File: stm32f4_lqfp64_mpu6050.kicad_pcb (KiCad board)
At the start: 4 copper layers, 130 x 100 mm, 170 parts, among them M5 ALIS-CUSTOM-PARTS_POWERPADS, P1 CONN_01X08, P2 CONN_02X08, Q5 BSS138, Q6 CRYSTAL_50X32, U1 STM32F405R, U2 MPU6050, U3 LP2985LV, U4 LP2985LV, U5 W25Q80BV, U6 LM1881, U7 TS5A3160, U8 TS5A3160, X1 CON-JST_SM04B-SRSS-TB, X2 CON-JST_SM04B-SRSS-TB, X4 CON-JST_SM04B-SRSS-TB

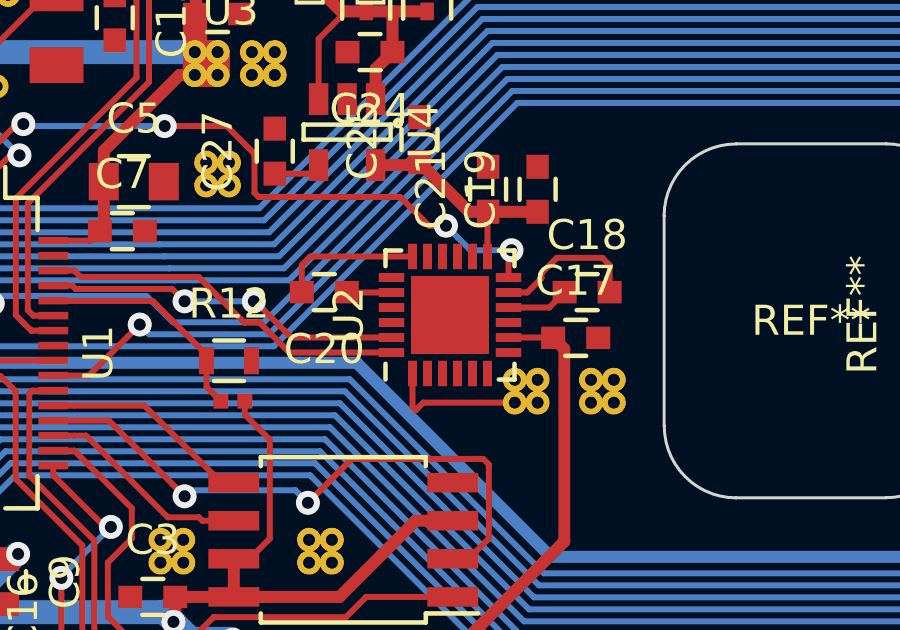
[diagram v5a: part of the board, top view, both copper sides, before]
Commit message: deleted the ground pad under the mpu6050
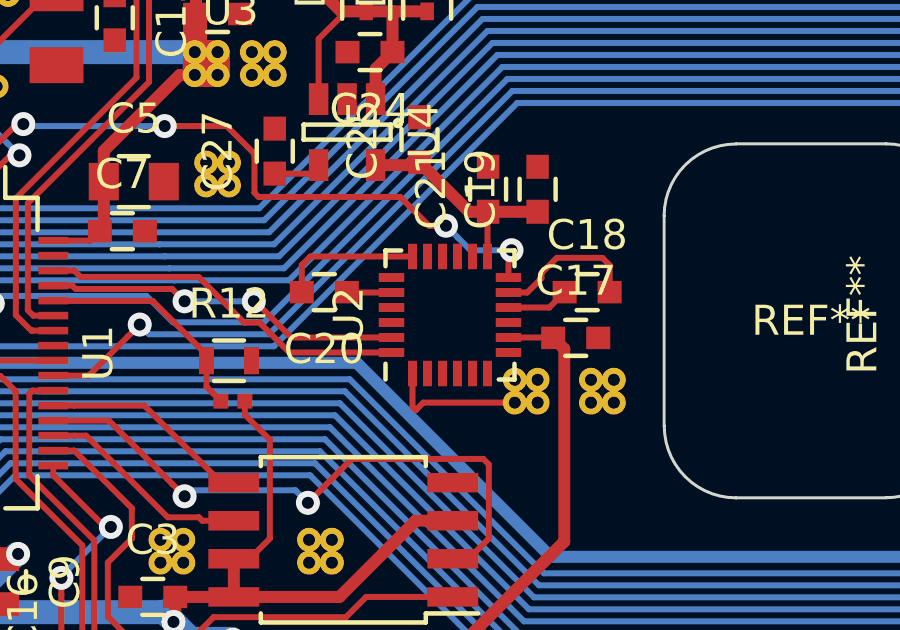
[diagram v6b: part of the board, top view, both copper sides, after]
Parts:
- U2: footprint Housings_DFN_QFN:QFN-24-1EP_4x4mm_Pitch0.5mm -> QFN-24_4x4mm_Pitch0.5mm
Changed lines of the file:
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@@
     (add_net VBAT)
+  )
+  (module QFN-24_4x4mm_Pitch0.5mm (layer Top)
+    (at 132.08 104.775 90)
+    (descr "24-Lead Plastic Quad Flat, No Lead Package (MJ) - 4x4x0.9 mm Body [QFN]; (see Microchip Packaging Specification 00000049BS.pdf)")
+    (tags "QFN 0.5")
+    (attr smd)
+    (fp_text reference U2 (at 0 -3.375 90) (layer F.SilkS)
+      (effects (font (size 1 1) (thickness 0.15)))
+    )
+    (fp_text value MPU6050 (at 0 3.375 90) (layer F.Fab)
+      (effects (font (size 1 1) (thickness 0.15)))
+    )
+    (fp_line (start -2.65 -2.65) (end -2.65 2.65) (layer F.CrtYd) (width 0.05))
+    (fp_line (start 2.65 -2.65) (end 2.65 2.65) (layer F.CrtYd) (width 0.05))
+    (fp_line (start -2.65 -2.65) (end 2.65 -2.65) (layer F.CrtYd) (width 0.05))
+    (fp_line (start -2.65 2.65) (end 2.65 2.65) (layer F.CrtYd) (width 0.05))
+    (fp_line (start 2.15 -2.15) (end 2.15 -1.625) (layer F.SilkS) (width 0.15))
+    (fp_line (start -2.15 2.15) (end -2.15 1.625) (layer F.SilkS) (width 0.15))
+    (fp_line (start 2.15 2.15) (end 2.15 1.625) (layer F.SilkS) (width 0.15))
+    (fp_line (start -2.15 -2.15) (end -1.625 -2.15) (layer F.SilkS) (width 0.15))
+    (fp_line (start -2.15 2.15) (end -1.625 2.15) (layer F.SilkS) (width 0.15))
+    (fp_line (start 2.15 2.15) (end 1.625 2.15) (layer F.SilkS) (width 0.15))
+    (fp_line (start 2.15 -2.15) (end 1.625 -2.15) (layer F.SilkS) (width 0.15))
+    (pad 1 smd rect (at -1.95 -1.25 90) (size 0.85 0.3) (layers Top F.Paste F.Mask)
+      (net 1 GND))
+    (pad 2 smd rect (at -1.95 -0.75 90) (size 0.85 0.3) (layers Top F.Paste F.Mask)
+      (net 68 "Net-(U2-Pad2)"))
+    (pad 3 smd rect (at -1.95 -0.25 90) (size 0.85 0.3) (layers Top F.Paste F.Mask)
+      (net 69 "Net-(U2-Pad3)"))
+    (pad 4 smd rect (at -1.95 0.25 90) (size 0.85 0.3) (layers Top F.Paste F.Mask)
+      (net 70 "Net-(U2-Pad4)"))
+    (pad 5 smd rect (at -1.95 0.75 90) (size 0.85 0.3) (layers Top F.Paste F.Mask)
+      (net 71 "Net-(U2-Pad5)"))
+    (pad 6 smd rect (at -1.95 1.25 90) (size 0.85 0.3) (layers Top F.Paste F.Mask)
+      (net 72 "Net-(U2-Pad6)"))
+    (pad 7 smd rect (at -1.25 1.95 180) (size 0.85 0.3) (layers Top F.Paste F.Mask)
+      (net 73 "Net-(U2-Pad7)"))
+    (pad 8 smd rect (at -0.75 1.95 180) (size 0.85 0.3) (layers Top F.Paste F.Mask)
+      (net 3 3.3V))
+    (pad 9 smd rect (at -0.25 1.95 180) (size 0.85 0.3) (layers Top F.Paste F.Mask)
+      (net 74 "Net-(U2-Pad9)"))
+    (pad 10 smd rect (at 0.25 1.95 180) (size 0.85 0.3) (layers Top F.Paste F.Mask)
+      (net 9 "Net-(C18-Pad1)"))
+    (pad 11 smd rect (at 0.75 1.95 180) (size 0.85 0.3) (layers Top F.Paste F.Mask)
+      (net 1 GND))
+    (pad 12 smd rect (at 1.25 1.95 180) (size 0.85 0.3) (layers Top F.Paste F.Mask)
+      (net 37 IMU_INT))
+    (pad 13 smd rect (at 1.95 1.25 90) (size 0.85 0.3) (layers Top F.Paste F.Mask)
+      (net 10 3.3V_SEN))
+    (pad 14 smd rect (at 1.95 0.75 90) (size 0.85 0.3) (layers Top F.Paste F.Mask)
+      (net 75 "Net-(U2-Pad14)"))
+    (pad 15 smd rect (at 1.95 0.25 90) (size 0.85 0.3) (layers Top F.Paste F.Mask)
+      (net 76 "Net-(U2-Pad15)"))
+    (pad 16 smd rect (at 1.95 -0.25 90) (size 0.85 0.3) (layers Top F.Paste F.Mask)
+      (net 77 "Net-(U2-Pad16)"))
+    (pad 17 smd rect (at 1.95 -0.75 90) (size 0.85 0.3) (layers Top F.Paste F.Mask)
+      (net 78 "Net-(U2-Pad17)"))
+    (pad 18 smd rect (at 1.95 -1.25 90) (size 0.85 0.3) (layers Top F.Paste F.Mask)
+      (net 1 GND))
+    (pad 19 smd rect (at 1.25 -1.95 180) (size 0.85 0.3) (layers Top F.Paste F.Mask)
+      (net 79 "Net-(U2-Pad19)"))
+    (pad 20 smd rect (at 0.75 -1.95 180) (size 0.85 0.3) (layers Top F.Paste F.Mask)
+      (net 11 "Net-(C20-Pad1)"))
+    (pad 21 smd rect (at 0.25 -1.95 180) (size 0.85 0.3) (layers Top F.Paste F.Mask)
+      (net 80 "Net-(U2-Pad21)"))
+    (pad 22 smd rect (at -0.25 -1.95 180) (size 0.85 0.3) (layers Top F.Paste F.Mask)
+      (net 81 "Net-(U2-Pad22)"))
+    (pad 23 smd rect (at -0.75 -1.95 180) (size 0.85 0.3) (layers Top F.Paste F.Mask)
+      (net 66 SCL))
+    (pad 24 smd rect (at -1.25 -1.95 180) (size 0.85 0.3) (layers Top F.Paste F.Mask)
+      (net 67 SDA))
+    (model Housings_DFN_QFN.3dshapes/QFN-24-1EP_4x4mm_Pitch0.5mm.wrl
+      (at (xyz 0 0 0))
+      (scale (xyz 1 1 1))
+      (rotate (xyz 0 0 0))
+    )
   )
   (module alis_parts:via_04 (layer Top)
@@
       (at (xyz 0 0 0))
       (scale (xyz 1 1 1))
-      (rotate (xyz 0 0 0))
-    )
-  )
-  (module Housings_DFN_QFN:QFN-24-1EP_4x4mm_Pitch0.5mm (layer Top)
-    (at 132.08 104.775 90)
-    (descr "24-Lead Plastic Quad Flat, No Lead Package (MJ) - 4x4x0.9 mm Body [QFN]; (see Microchip Packaging Specification 00000049BS.pdf)")
-    (tags "QFN 0.5")
-    (attr smd)
-    (fp_text reference U2 (at 0 -3.375 90) (layer F.SilkS)
-      (effects (font (size 1 1) (thickness 0.15)))
-    )
-    (fp_text value MPU6050 (at 0 3.375 90) (layer F.Fab)
-      (effects (font (size 1 1) (thickness 0.15)))
-    )
-    (fp_line (start -2.65 -2.65) (end -2.65 2.65) (layer F.CrtYd) (width 0.05))
-    (fp_line (start 2.65 -2.65) (end 2.65 2.65) (layer F.CrtYd) (width 0.05))
-    (fp_line (start -2.65 -2.65) (end 2.65 -2.65) (layer F.CrtYd) (width 0.05))
-    (fp_line (start -2.65 2.65) (end 2.65 2.65) (layer F.CrtYd) (width 0.05))
-    (fp_line (start 2.15 -2.15) (end 2.15 -1.625) (layer F.SilkS) (width 0.15))
-    (fp_line (start -2.15 2.15) (end -2.15 1.625) (layer F.SilkS) (width 0.15))
-    (fp_line (start 2.15 2.15) (end 2.15 1.625) (layer F.SilkS) (width 0.15))
-    (fp_line (start -2.15 -2.15) (end -1.625 -2.15) (layer F.SilkS) (width 0.15))
-    (fp_line (start -2.15 2.15) (end -1.625 2.15) (layer F.SilkS) (width 0.15))
-    (fp_line (start 2.15 2.15) (end 1.625 2.15) (layer F.SilkS) (width 0.15))
-    (fp_line (start 2.15 -2.15) (end 1.625 -2.15) (layer F.SilkS) (width 0.15))
-    (pad 1 smd rect (at -1.95 -1.25 90) (size 0.85 0.3) (layers Top F.Paste F.Mask)
-      (net 1 GND))
-    (pad 2 smd rect (at -1.95 -0.75 90) (size 0.85 0.3) (layers Top F.Paste F.Mask)
-      (net 68 "Net-(U2-Pad2)"))
-    (pad 3 smd rect (at -1.95 -0.25 90) (size 0.85 0.3) (layers Top F.Paste F.Mask)
-      (net 69 "Net-(U2-Pad3)"))
-    (pad 4 smd rect (at -1.95 0.25 90) (size 0.85 0.3) (layers Top F.Paste F.Mask)
-      (net 70 "Net-(U2-Pad4)"))
-    (pad 5 smd rect (at -1.95 0.75 90) (size 0.85 0.3) (layers Top F.Paste F.Mask)
-      (net 71 "Net-(U2-Pad5)"))
-    (pad 6 smd rect (at -1.95 1.25 90) (size 0.85 0.3) (layers Top F.Paste F.Mask)
-      (net 72 "Net-(U2-Pad6)"))
-    (pad 7 smd rect (at -1.25 1.95 180) (size 0.85 0.3) (layers Top F.Paste F.Mask)
-      (net 73 "Net-(U2-Pad7)"))
-    (pad 8 smd rect (at -0.75 1.95 180) (size 0.85 0.3) (layers Top F.Paste F.Mask)
-      (net 3 3.3V))
-    (pad 9 smd rect (at -0.25 1.95 180) (size 0.85 0.3) (layers Top F.Paste F.Mask)
-      (net 74 "Net-(U2-Pad9)"))
-    (pad 10 smd rect (at 0.25 1.95 180) (size 0.85 0.3) (layers Top F.Paste F.Mask)
-      (net 9 "Net-(C18-Pad1)"))
-    (pad 11 smd rect (at 0.75 1.95 180) (size 0.85 0.3) (layers Top F.Paste F.Mask)
-      (net 1 GND))
-    (pad 12 smd rect (at 1.25 1.95 180) (size 0.85 0.3) (layers Top F.Paste F.Mask)
-      (net 37 IMU_INT))
-    (pad 13 smd rect (at 1.95 1.25 90) (size 0.85 0.3) (layers Top F.Paste F.Mask)
-      (net 10 3.3V_SEN))
-    (pad 14 smd rect (at 1.95 0.75 90) (size 0.85 0.3) (layers Top F.Paste F.Mask)
-      (net 75 "Net-(U2-Pad14)"))
-    (pad 15 smd rect (at 1.95 0.25 90) (size 0.85 0.3) (layers Top F.Paste F.Mask)
-      (net 76 "Net-(U2-Pad15)"))
-    (pad 16 smd rect (at 1.95 -0.25 90) (size 0.85 0.3) (layers Top F.Paste F.Mask)
-      (net 77 "Net-(U2-Pad16)"))
-    (pad 17 smd rect (at 1.95 -0.75 90) (size 0.85 0.3) (layers Top F.Paste F.Mask)
-      (net 78 "Net-(U2-Pad17)"))
-    (pad 18 smd rect (at 1.95 -1.25 90) (size 0.85 0.3) (layers Top F.Paste F.Mask)
-      (net 1 GND))
-    (pad 19 smd rect (at 1.25 -1.95 180) (size 0.85 0.3) (layers Top F.Paste F.Mask)
-      (net 79 "Net-(U2-Pad19)"))
-    (pad 20 smd rect (at 0.75 -1.95 180) (size 0.85 0.3) (layers Top F.Paste F.Mask)
-      (net 11 "Net-(C20-Pad1)"))
-    (pad 21 smd rect (at 0.25 -1.95 180) (size 0.85 0.3) (layers Top F.Paste F.Mask)
-      (net 80 "Net-(U2-Pad21)"))
-    (pad 22 smd rect (at -0.25 -1.95 180) (size 0.85 0.3) (layers Top F.Paste F.Mask)
-      (net 81 "Net-(U2-Pad22)"))
-    (pad 23 smd rect (at -0.75 -1.95 180) (size 0.85 0.3) (layers Top F.Paste F.Mask)
-      (net 66 SCL))
-    (pad 24 smd rect (at -1.25 -1.95 180) (size 0.85 0.3) (layers Top F.Paste F.Mask)
-      (net 67 SDA))
-    (pad 25 smd rect (at 0.65 0.65 90) (size 1.3 1.3) (layers Top F.Paste F.Mask)
-      (solder_paste_margin_ratio -0.2))
-    (pad 25 smd rect (at 0.65 -0.65 90) (size 1.3 1.3) (layers Top F.Paste F.Mask)
-      (solder_paste_margin_ratio -0.2))
-    (pad 25 smd rect (at -0.65 0.65 90) (size 1.3 1.3) (layers Top F.Paste F.Mask)
-      (solder_paste_margin_ratio -0.2))
-    (pad 25 smd rect (at -0.65 -0.65 90) (size 1.3 1.3) (layers Top F.Paste F.Mask)
-      (solder_paste_margin_ratio -0.2))
-    (model Housings_DFN_QFN.3dshapes/QFN-24-1EP_4x4mm_Pitch0.5mm.wrl
-      (at (xyz 0 0 0))
-      (scale (xyz 1 1 1))

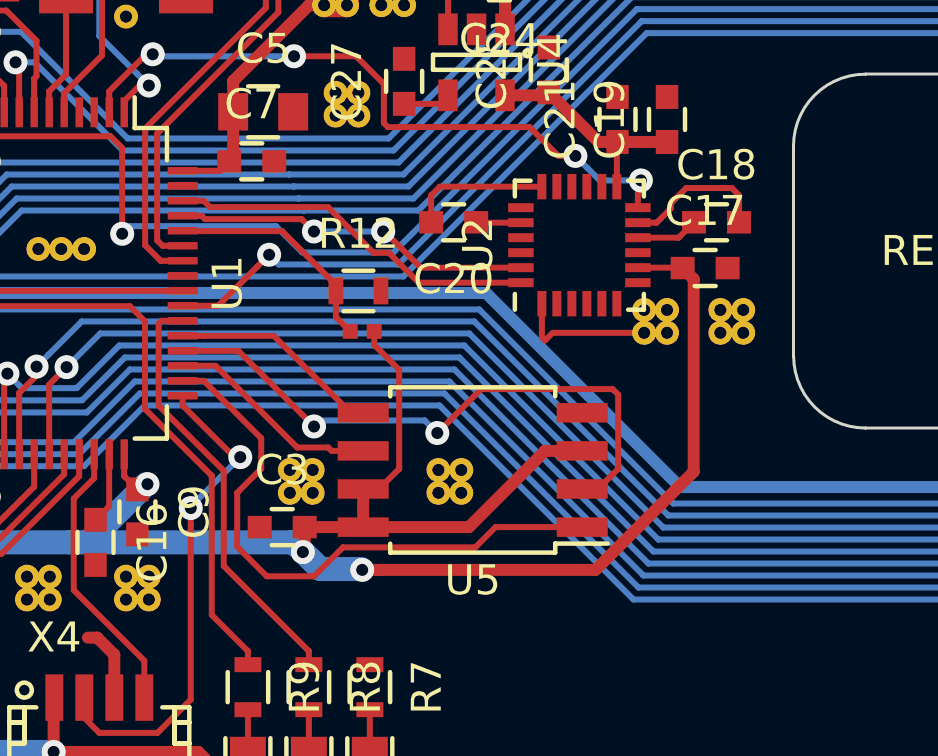
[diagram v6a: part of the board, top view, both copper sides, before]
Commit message: added I2C pullups and pulled MPU6050 AD0 to GND (DOH)
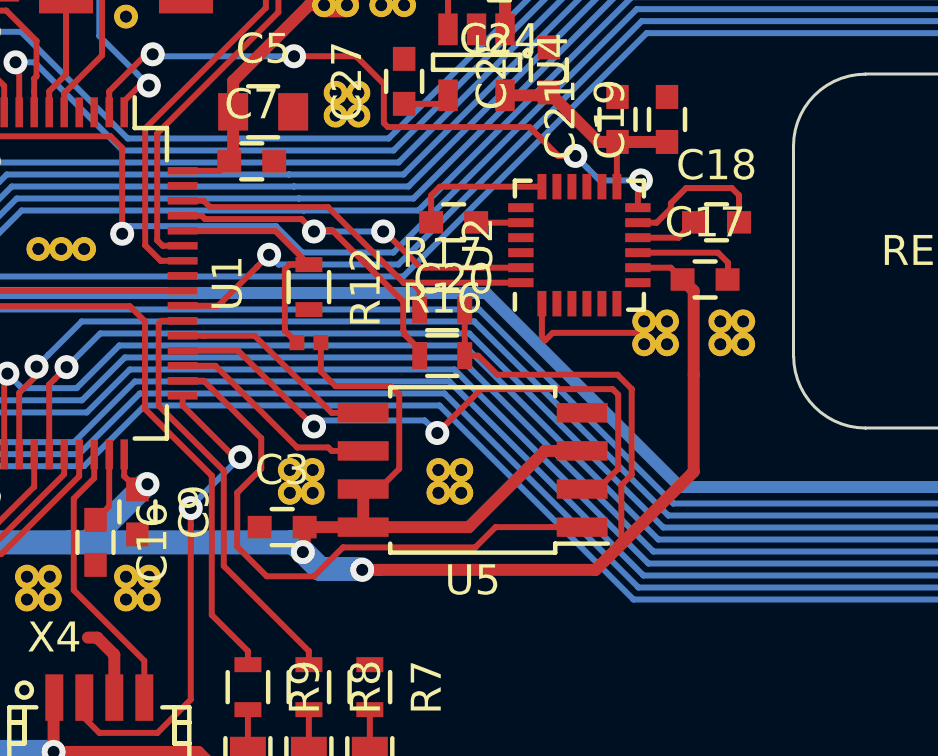
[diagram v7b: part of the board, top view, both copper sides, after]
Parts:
- added R16: 22k, Resistors_SMD:R_0603, F.Cu at (127.5, 108.5)
- added R17: 22k, Resistors_SMD:R_0603, F.Cu at (127.5, 106.9)
- ?: footprint alis_parts:via_04 -> via_04_no_front_mask
- ? (x88): footprint alis_parts:via_04 -> alis_parts:via_04_no_front_mask
- moved JP2 1.82 mm to (123.1, 108.1)
- moved R12 1.66 mm to (123.1, 106.2), turned to 270 degrees
- moved ? 0.38 mm to (136.8, 108.1)
- moved ? 0.38 mm to (137.5, 108.1)
- moved ? 0.38 mm to (137.5, 107.3)
- moved ? 0.38 mm to (136.8, 107.3)
- moved ? 0.38 mm to (134.2, 108.1)
- moved ? 0.38 mm to (134.2, 107.3)
- moved ? 0.38 mm to (135.0, 107.3)
- moved ? 0.38 mm to (135.0, 108.1)
- moved C17 0.38 mm to (136.3, 105.9)
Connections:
- U2 pad 9: Net-(U2-Pad9) -> GND
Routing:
- net 3.3V: track 250.9 -> 265.0 mm
- net SCL: track 12.0 -> 18.0 mm
- net GND: track 28.5 -> 32.2 mm
- net SDA: track 12.4 -> 13.7 mm
- net Net-(JP2-Pad2): track 7.60 -> 8.16 mm
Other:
- board text added: "Flexi Main"
